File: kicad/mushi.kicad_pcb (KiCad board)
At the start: 2 copper layers, 261 x 90.8 mm, 86 parts

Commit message: new
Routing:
- net thumbs_middle_cluster: track 74.9 -> 83.3 mm
- net thumbs_outer_cluster: track 55.4 -> 62.4 mm
- net matrix_ring_middle: track 103.1 -> 109.2 mm
- net matrix_pinky_middle: track 124.2 -> 130.3 mm
- net matrix_middle_middle: track 83.5 -> 89.4 mm
- net matrix_index_middle: track 59.4 -> 65.3 mm
- net matrix_outer_middle: track 34.7 -> 40.5 mm
- net RX: track 31.7 -> 34.9 mm
- net TX: track 33.4 -> 35.6 mm
- net matrix_pinky_top: track 127.1 -> 129.3 mm
- net matrix_ring_top: track 103.9 -> 105.8 mm
- net matrix_middle_top: track 86.0 -> 87.4 mm
- net matrix_index_top: track 62.3 -> 63.5 mm
- net matrix_outer_top: track 39.9 -> 41.1 mm

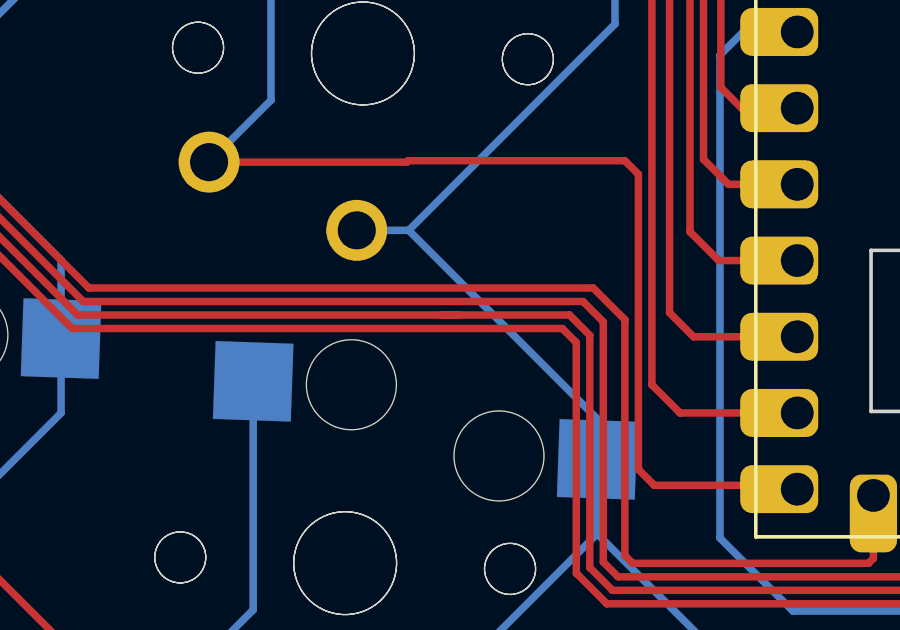
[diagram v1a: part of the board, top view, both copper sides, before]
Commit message: remove empty segment
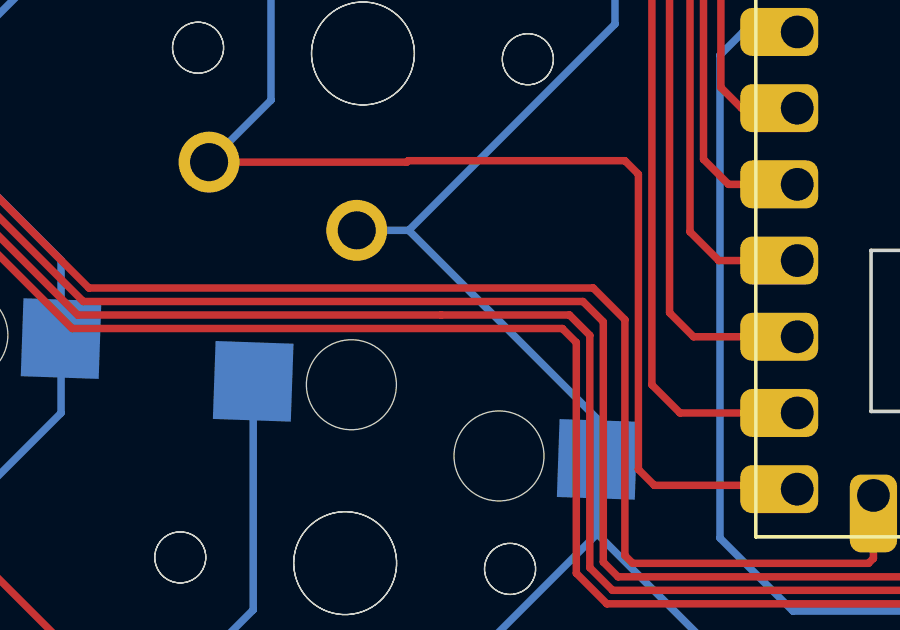
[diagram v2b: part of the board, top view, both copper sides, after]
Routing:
- net matrix_ring_middle: track 109.2 -> 108.7 mm
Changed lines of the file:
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@@
   (segment (start 75.644036 58.42) (end 83.264036 66.04) (width 0.25) (layer "F.Cu") (net 6))
   (segment (start 44.43495 59.468233) (end 45.483183 58.42) (width 0.25) (layer "F.Cu") (net 6))
-  (segment (start 106.71 70.462978) (end 107.290186 70.462978) (width 0.25) (layer "F.Cu") (net 6))
   (segment (start 125.37 79.64) (end 126.19495 78.81505) (width 0.25) (layer "F.Cu") (net 6))
   (segment (start 90.167208 66.04) (end 94.590186 70.462978) (width 0.25) (layer "F.Cu") (net 6))

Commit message: cleanup
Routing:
- net mirror_matrix_pinky_top: track 110.4 -> 127.0 mm
- net mirror_matrix_middle_top: track 70.0 -> 82.7 mm
- net mirror_matrix_ring_top: track 87.5 -> 96.8 mm
- net mirror_matrix_index_top: track 46.7 -> 54.7 mm
- net mirror_matrix_middle_middle: track 69.7 -> 77.2 mm
- net mirror_matrix_ring_middle: track 88.8 -> 96.0 mm
- net mirror_matrix_pinky_middle: track 112.9 -> 119.5 mm
- net mirror_matrix_index_middle: track 44.9 -> 50.6 mm
- net mirror_matrix_ring_bottom: track 106.2 -> 111.8 mm
- net mirror_matrix_outer_middle: track 23.3 -> 27.7 mm
- net mirror_matrix_middle_bottom: track 81.2 -> 85.2 mm
- net mirror_matrix_index_bottom: track 57.9 -> 61.8 mm
- net mirror_thumbs_inner_cluster: track 92.5 -> 95.6 mm
- net mirror_thumbs_middle_cluster: track 73.6 -> 76.1 mm
- net mirror_matrix_outer_bottom: track 33.5 -> 36.0 mm
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
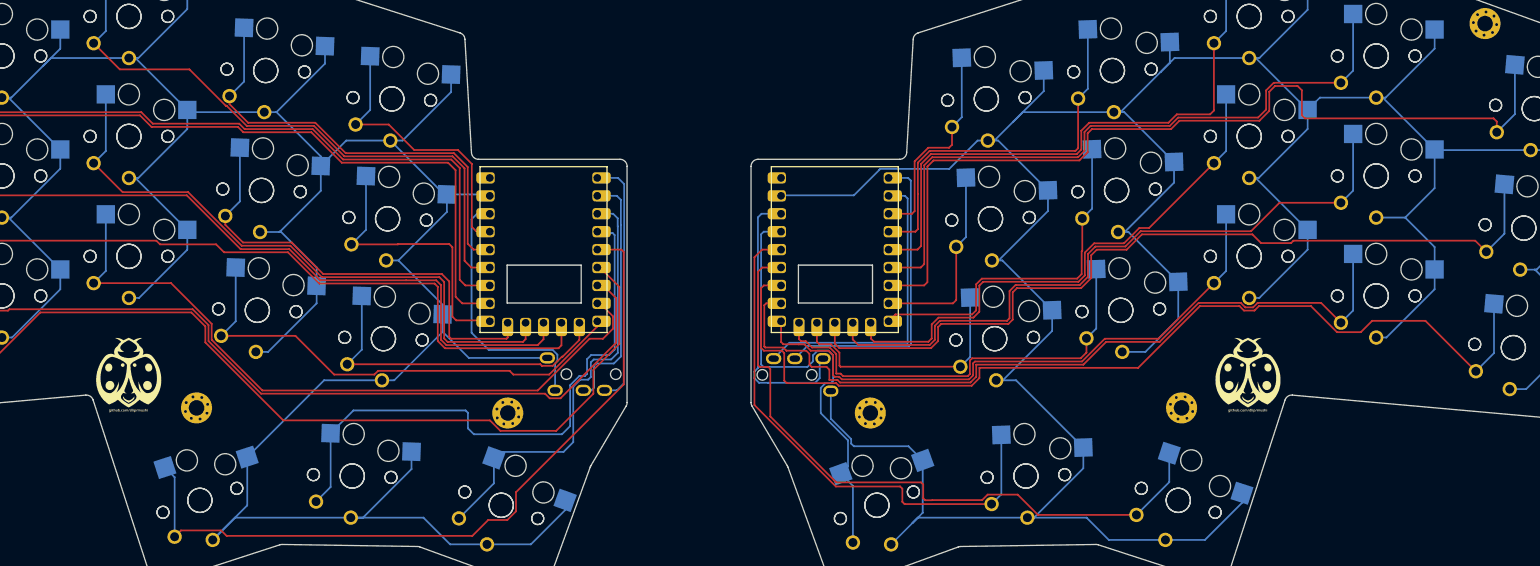
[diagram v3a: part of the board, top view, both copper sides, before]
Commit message: smooth right side
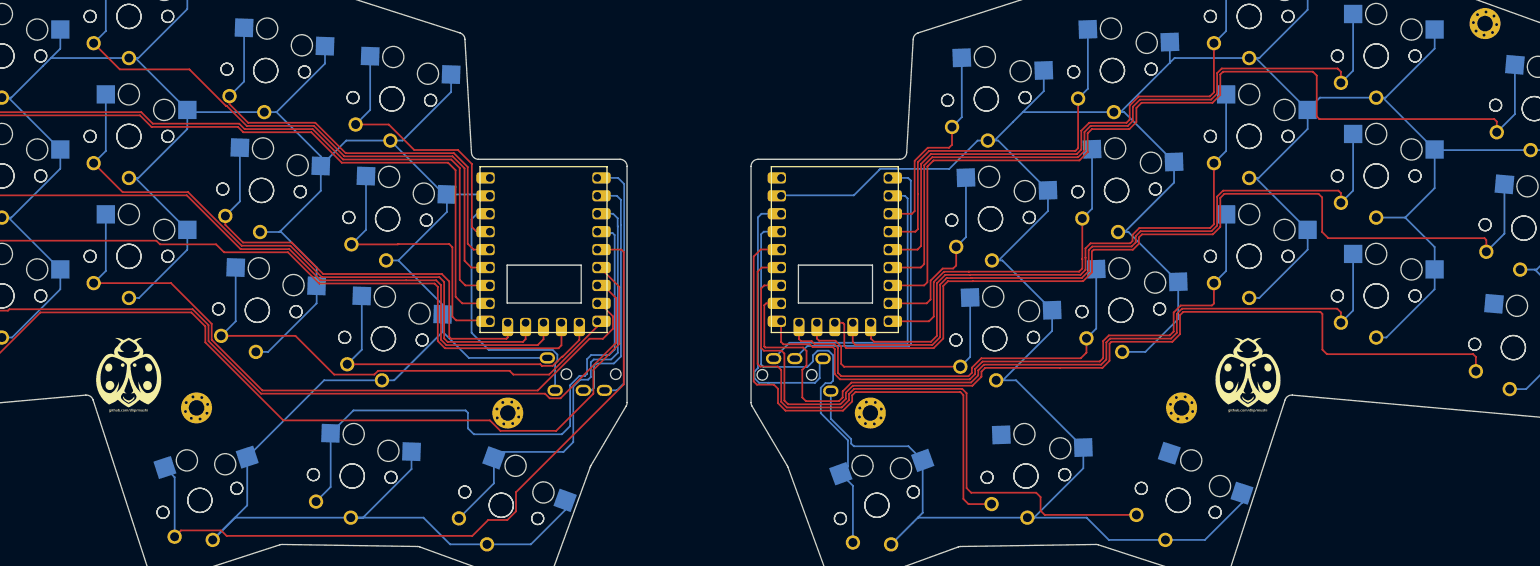
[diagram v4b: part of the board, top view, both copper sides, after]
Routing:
- net mirror_matrix_pinky_middle: track 119.5 -> 131.6 mm
- net mirror_matrix_ring_bottom: track 111.8 -> 119.5 mm
- net mirror_matrix_middle_middle: track 77.2 -> 83.7 mm
- net mirror_matrix_ring_middle: track 96.0 -> 102.2 mm
- net mirror_matrix_middle_bottom: track 85.2 -> 89.8 mm
- net mirror_matrix_pinky_top: track 127.0 -> 131.3 mm
- net rGND: track 520.6 -> 516.6 mm
- net mirror_matrix_ring_top: track 96.8 -> 100.7 mm
- net mirror_matrix_pinky_bottom: track 139.1 -> 136.9 mm
- net mirror_thumbs_inner_cluster: track 95.6 -> 93.5 mm
- net GND: track 501.2 -> 499.6 mm
- net mirror_matrix_outer_middle: track 27.7 -> 26.4 mm
- net mirror_thumbs_middle_cluster: track 76.1 -> 75.4 mm

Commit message: cleanup left side
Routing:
- net matrix_pinky_middle: track 130.3 -> 144.4 mm
- net thumbs_inner_cluster: track 107.9 -> 121.2 mm
- net matrix_ring_bottom: track 123.0 -> 136.3 mm
- net matrix_pinky_bottom: track 153.3 -> 166.5 mm
- net matrix_pinky_top: track 129.3 -> 141.7 mm
- net matrix_middle_bottom: track 100.1 -> 112.2 mm
- net mirror_thumbs_inner_cluster: track 93.5 -> 104.2 mm
- net mirror_matrix_pinky_bottom: track 136.9 -> 147.6 mm
- net mirror_thumbs_middle_cluster: track 75.4 -> 85.8 mm
- net matrix_middle_middle: track 89.4 -> 95.6 mm
- net matrix_ring_middle: track 108.7 -> 114.6 mm
- net matrix_middle_top: track 87.4 -> 92.9 mm
- net matrix_index_bottom: track 70.1 -> 75.6 mm
- net matrix_ring_top: track 105.8 -> 111.1 mm
- net matrix_index_middle: track 65.3 -> 67.7 mm
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
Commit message: clean up gnd
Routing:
- net rGND: track 516.6 -> 603.9 mm
- net GND: track 499.6 -> 573.6 mm
- net mirror_thumbs_inner_cluster: track 104.2 -> 109.3 mm
- net mirror_thumbs_outer_cluster: track 63.9 -> 65.9 mm
- net P3V3: track 37.6 -> 38.9 mm
- net thumbs_outer_cluster: track 62.4 -> 63.6 mm
- net mirror_matrix_pinky_top: track 131.3 -> 132.4 mm
- net mirror_matrix_pinky_bottom: track 147.6 -> 148.7 mm
- net rP3V3: track 39.2 -> 40.2 mm
- net rRX: track 43.2 -> 43.9 mm
- net matrix_ring_bottom: track 136.3 -> 137.0 mm
- net mirror_matrix_ring_top: track 100.7 -> 101.3 mm
- net mirror_matrix_middle_top: track 82.3 -> 82.9 mm
- net matrix_middle_middle: track 95.6 -> 96.1 mm

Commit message: more cleanup
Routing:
- net GND: track 573.6 -> 557.0 mm
- net rGND: track 603.9 -> 594.9 mm
- net thumbs_inner_cluster: track 121.2 -> 126.5 mm
- net thumbs_outer_cluster: track 63.6 -> 67.8 mm
- net mirror_matrix_pinky_middle: track 131.6 -> 132.6 mm
- net matrix_index_top: track 64.9 -> 65.8 mm
- net matrix_outer_top: track 43.4 -> 44.3 mm
- net matrix_index_bottom: track 75.6 -> 76.4 mm
- net mirror_matrix_ring_bottom: track 119.5 -> 120.2 mm
- net matrix_ring_top: track 111.1 -> 111.8 mm
- net mirror_matrix_ring_middle: track 102.2 -> 102.8 mm
- net mirror_matrix_middle_middle: track 83.7 -> 84.4 mm
- net matrix_middle_top: track 92.9 -> 93.5 mm
- net mirror_matrix_middle_bottom: track 89.8 -> 90.4 mm
- net mirror_thumbs_outer_cluster: track 65.9 -> 66.4 mm

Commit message: cleanup
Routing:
- net matrix_outer_middle: track 39.5 -> 40.4 mm
- net matrix_index_middle: track 67.7 -> 68.5 mm
- net thumbs_middle_cluster: track 83.3 -> 84.0 mm
- net matrix_middle_bottom: track 112.2 -> 112.9 mm
